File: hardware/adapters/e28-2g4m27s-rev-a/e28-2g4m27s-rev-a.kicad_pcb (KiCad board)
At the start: 2 copper layers, 84 x 80 mm, 39 parts, among them J1 TSW-110-07-G-S, J2 TSW-108-07-G-S, U1 E28-2G4M27S, U2 AP63203WU-7

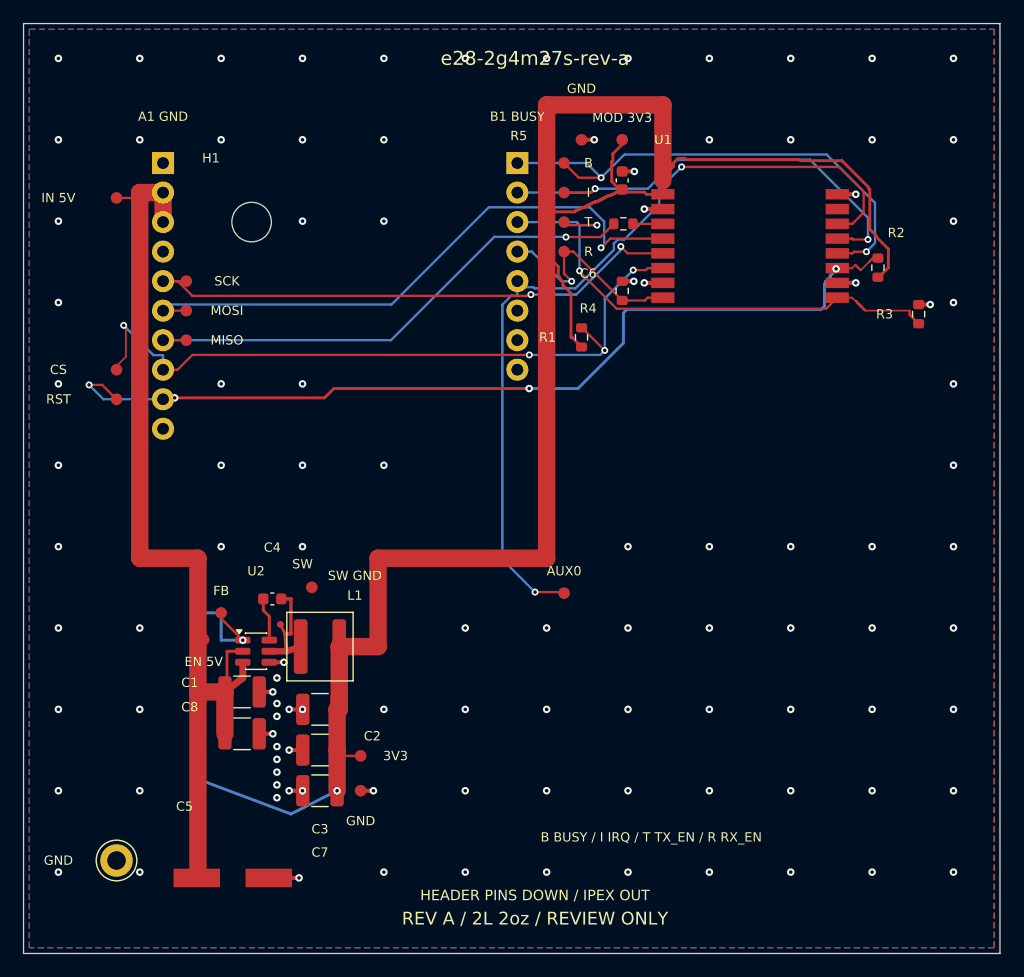
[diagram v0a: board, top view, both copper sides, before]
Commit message: Improve Rev-A ground references and feedback routing
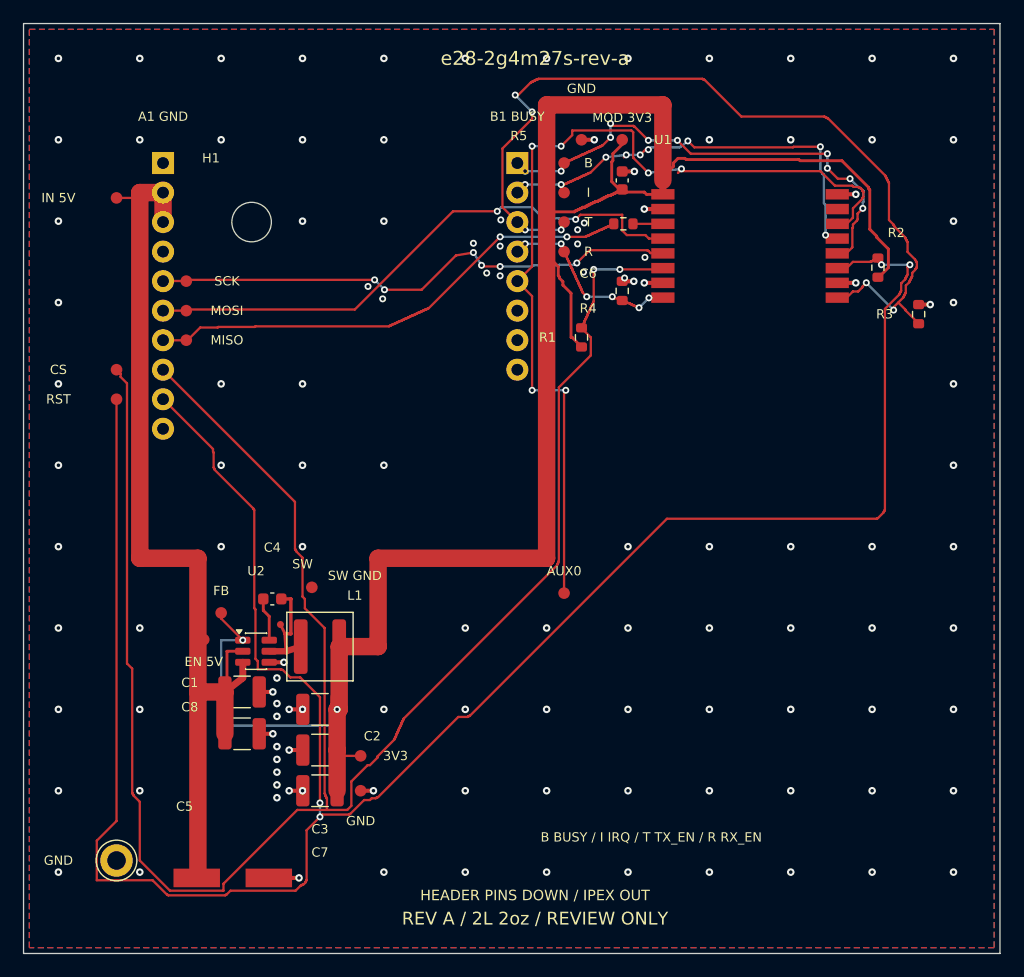
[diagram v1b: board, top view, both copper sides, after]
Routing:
- net /RESET_N: track 79.5 -> 199.0 mm
- net /CS_N: track 62.1 -> 171.0 mm, vias 4 -> 2
- net /TX_EN: track 46.4 -> 76.3 mm, vias 2 -> 6
- net /RADIO_3V3: track 190.5 -> 177.6 mm
- net /AUX0: track 71.9 -> 80.4 mm, vias 2 -> 6
- net /SPI_MOSI: track 51.9 -> 48.9 mm, vias 1 -> 2
- net /IRQ: track 40.8 -> 38.4 mm, vias 2 -> 9
- net /RX_EN: track 18.9 -> 16.8 mm, vias 1 -> 6
- net /SPI_MISO: track 44.9 -> 42.9 mm, vias 1 -> 2
- net /BUSY: track 44.6 -> 42.6 mm, vias 2 -> 10
- net /SPI_SCK: track 47.7 -> 46.0 mm, vias 2 -> 6
- net /GND: vias 108 -> 121
